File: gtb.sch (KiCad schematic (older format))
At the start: 7 parts, among them U1 7555

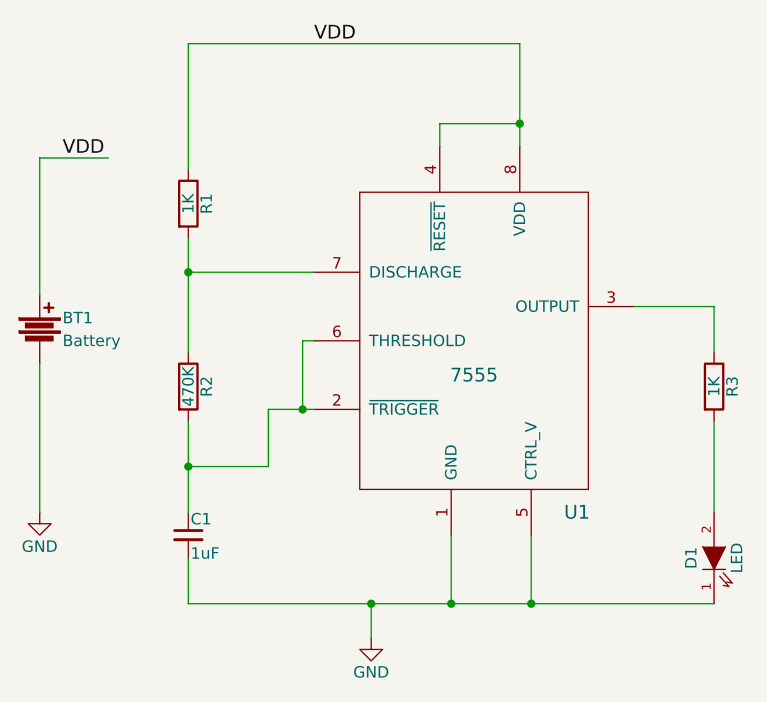
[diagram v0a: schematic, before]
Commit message: updated to remove Pin5 connection to ground and R3 to 100Ohm
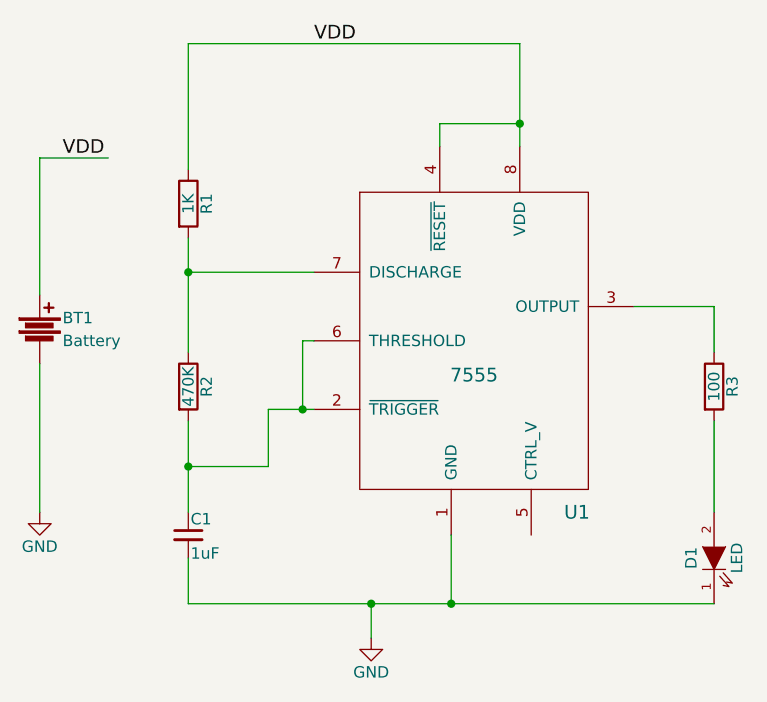
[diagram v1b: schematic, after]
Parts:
- R3: value 1K -> 100
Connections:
- wire segments 24 -> 23
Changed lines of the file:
@@
 P 6700 3750
 F 0 "R3" V 6780 3750 50  0000 C CNN
-F 1 "1K" V 6700 3750 50  0000 C CNN
+F 1 "100" V 6700 3750 50  0000 C CNN
 F 2 "Resistors_SMD:R_0805_HandSoldering" V 6630 3750 50  0001 C CNN
 F 3 "" H 6700 3750 50  0000 C CNN
@@
 	1    0    0    -1
 $EndComp
-Connection ~ 5900 4700
-Wire Wire Line
-	5900 4400 5900 4700
 Connection ~ 5850 2600
 Wire Wire Line
@@
 Connection ~ 5550 4700
 Wire Wire Line
-	5550 4400 5550 4700
+	5550 4700 5550 4400
 Wire Wire Line
 	4400 4700 4400 4500
@@
 	4750 3850 4750 4100
 Wire Wire Line
-	4950 3850 4750 3850
+	4750 3850 4950 3850
 Connection ~ 4400 3250
 Wire Wire Line
